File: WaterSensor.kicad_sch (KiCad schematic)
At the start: 8 parts, among them J2 Main, Q1 2N3904

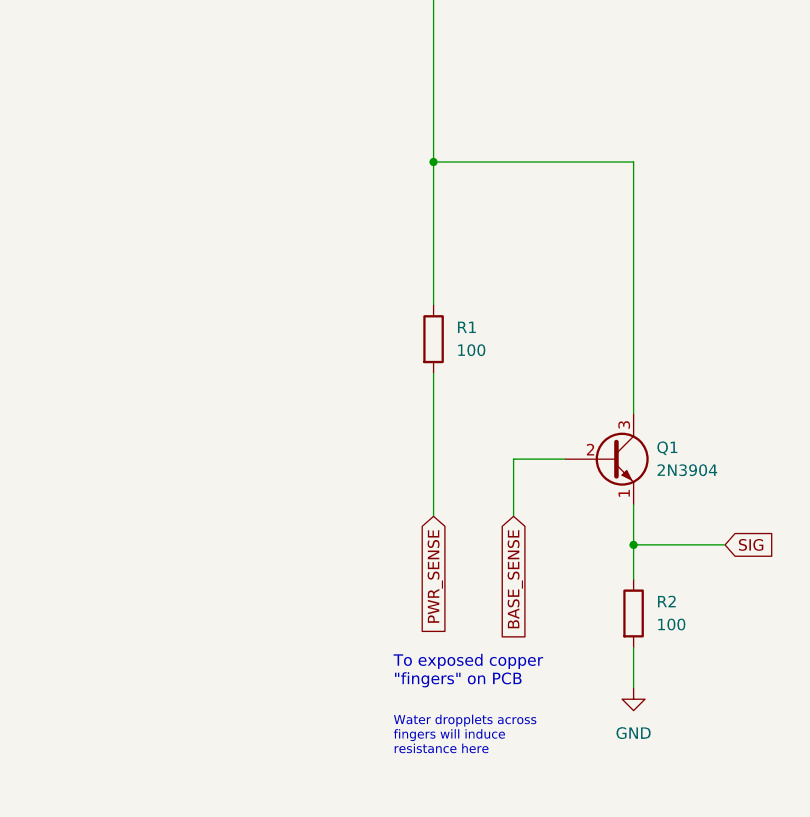
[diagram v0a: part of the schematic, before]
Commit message: Add pulldown resistor and update resistor values to bias a 3.3V output
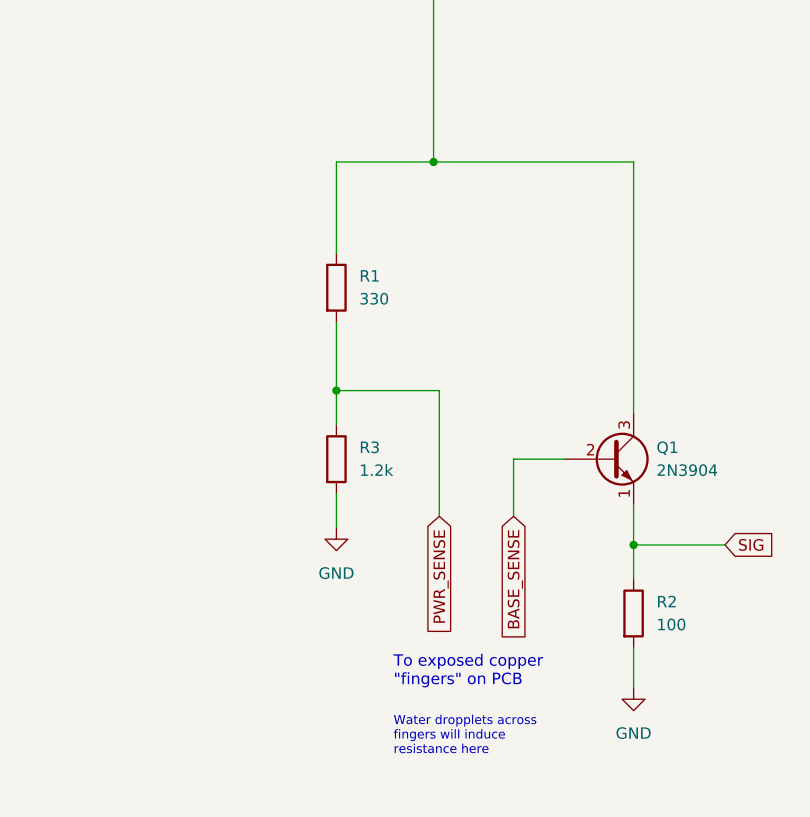
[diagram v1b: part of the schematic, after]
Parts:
- added R3: 1.2k, Resistor_THT:R_Axial_DIN0204_L3.6mm_D1.6mm_P1.90mm_Vertical, symbol Device:R
- R1: value 100 -> 330
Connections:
- net GND: now also R3.2
- net PWR_SENSE: now also R3.1
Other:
- moved on the sheet: R1

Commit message: Reverse changes as pulldown resistor is not needed
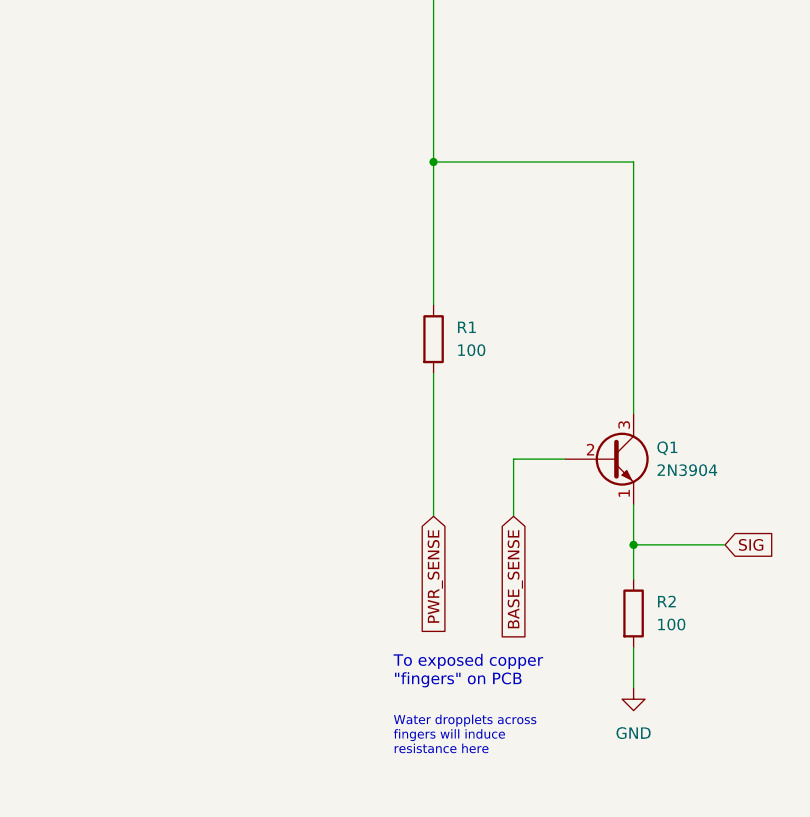
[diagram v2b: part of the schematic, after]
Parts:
- removed R3: 1.2k, Resistor_THT:R_Axial_DIN0204_L3.6mm_D1.6mm_P1.90mm_Vertical, symbol Device:R
- R1: value 330 -> 100
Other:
- moved on the sheet: R1
